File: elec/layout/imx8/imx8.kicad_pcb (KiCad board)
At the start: 2 copper layers, 67 parts, among them U1 _NXP_Semicon_MIMX8MM6CVTKZAA

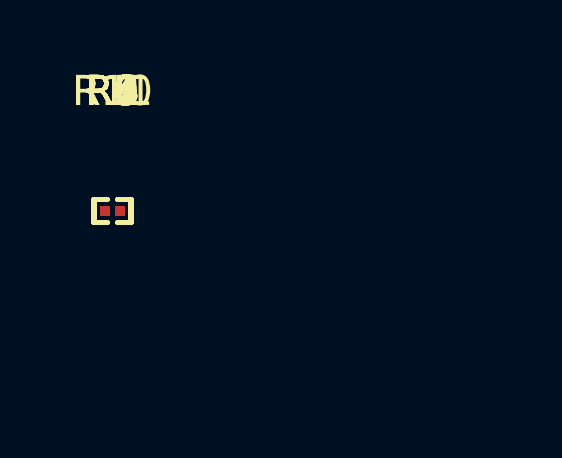
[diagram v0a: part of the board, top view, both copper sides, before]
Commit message: Update ato.yaml to build nonos + import into layout
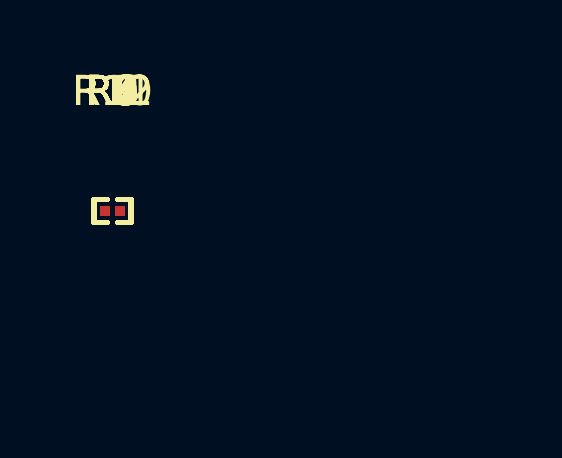
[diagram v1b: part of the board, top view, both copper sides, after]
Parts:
- added R12: 100kΩ ±1% 50mW, lcsc:R0201, F.Cu at (0.00, 0.00)
- R1: value 4.87kΩ ±1% 50mW -> 10kΩ ±1% 50mW
- R9: value 100kΩ ±1% 50mW -> 4.87kΩ ±1% 50mW
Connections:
- net *3E48.processor-net-5 renamed *7668-net-18
- net *3E48.processor.PMIC_ON_REQ-signal renamed *7668.ONOFF-signal
- net *3E48.processor.PMIC_STBY_REQ-signal renamed *7668.PMIC_ON_REQ-signal
- net NVCC_DRAM_1V1 renamed hv
- net NVCC_ENET renamed *7668-net-1
- net NVCC_SD2 renamed *7668-net-15
- net VDDA_1V8 renamed *7668-net-10
- net VDD_1V8 renamed net-0
- net VDD_3V3 renamed *7668-net-3
- net VDD_ARM_0V9 renamed *7668-net-5
- net VDD_DRAM_0V9 renamed *7668-net-2
- net VDD_PHY_0V9 renamed *7668-net-4
- net VDD_PHY_1V2 renamed *7668-net-7
- net VDD_SNVS_0V8 renamed net-1
- net VDD_SOC_0V8 renamed *7668-net-0
- net dram_ac02 renamed signal-40
- net dram_ac03 renamed signal-64
- net dram_ac04 renamed signal-8
- net dram_ac05 renamed signal-14
- net dram_ac08 renamed signal-28
- net dram_ac09 renamed signal-9
- net dram_ac10 renamed signal-43
- net dram_ac11 renamed signal-59
- net dram_ac12 renamed signal-5
- net dram_ac13 renamed signal-17
- net dram_ac22 renamed signal-18
- net dram_ac23 renamed signal-13
- net dram_ac24 renamed signal-37
- net dram_ac25 renamed signal-53
- net dram_ac28 renamed signal-62
- net dram_ac29 renamed signal-58
- net dram_ac30 renamed signal-32
- net dram_ac31 renamed signal-26
- net dram_ac32 renamed signal-65
- net dram_ac33 renamed signal-11
- net dram_dm0 renamed signal-4
- net dram_dm1 renamed signal-30
- net dram_dm2 renamed signal-22
- net dram_dm3 renamed signal-6
- net dram_dq00 renamed signal-16
- net dram_dq01 renamed signal-2
- net dram_dq02 renamed signal-23
- net dram_dq03 renamed signal-49
- net dram_dq04 renamed signal-31
- net dram_dq05 renamed signal-61
- net dram_dq06 renamed signal-55
- net dram_dq07 renamed signal-54
- net dram_dq08 renamed signal-10
- net dram_dq09 renamed signal-39
- net dram_dq10 renamed signal-38
- net dram_dq11 renamed signal-20
- net dram_dq12 renamed signal-56
- net dram_dq13 renamed signal-3
- net dram_dq14 renamed signal-47
- net dram_dq15 renamed signal-44
- net dram_dq16 renamed signal-7
- net dram_dq17 renamed signal-46
- net dram_dq18 renamed signal-66
- net dram_dq19 renamed signal-51
- net dram_dq20 renamed signal-25
- net dram_dq21 renamed signal-45
- net dram_dq22 renamed signal-33
- net dram_dq23 renamed signal-29
- net dram_dq24 renamed signal-21
- net dram_dq25 renamed signal-50
- net dram_dq26 renamed signal-1
- net dram_dq27 renamed signal-19
- net dram_dq28 renamed signal-15
- net dram_dq29 renamed signal-36
- net dram_dq30 renamed signal-60
- net dram_dq31 renamed signal-27
- net dram_dqs0_n renamed signal-67
- net dram_dqs0_p renamed signal-63
- net dram_dqs1_p renamed signal-41
- net dram_dqs3_n renamed signal-42
- net nand_ce1_b renamed *7668-signal
- net nand_ce2_b renamed signal-57
- net nand_ce3_b renamed signal-48
- net nand_cle renamed signal-0
- net nand_data04 renamed signal-34
- net nand_data05 renamed signal-24
- net nand_data06 renamed signal-52
- net nand_data07 renamed signal-12
- net nand_ready_b renamed signal-35
- C1 pad 2: GND -> lv
- C10 pad 2: GND -> lv
- C11 pad 2: GND -> lv
- C12 pad 1: *3E48.processor-hv -> *7668-hv
- C12 pad 2: GND -> lv
- C13 pad 2: GND -> lv
- C14 pad 2: GND -> lv
- C15 pad 2: GND -> lv
- C16 pad 2: GND -> lv
- C17 pad 2: GND -> lv
- C18 pad 2: GND -> lv
- C19 pad 2: GND -> lv
- C2 pad 2: GND -> lv
- C20 pad 2: GND -> lv
- C21 pad 2: GND -> lv
- C22 pad 2: GND -> lv
- C23 pad 2: GND -> lv
- C24 pad 2: GND -> lv
- C25 pad 2: GND -> lv
- C26 pad 2: GND -> lv
- C27 pad 2: GND -> lv
- C28 pad 2: GND -> lv
- C29 pad 2: GND -> lv
- C3 pad 2: GND -> lv
- C30 pad 2: GND -> lv
- C31 pad 2: GND -> lv
- C32 pad 2: GND -> lv
- C33 pad 2: GND -> lv
- C34 pad 2: GND -> lv
- C35 pad 2: GND -> lv
- C36 pad 2: GND -> lv
- C37 pad 2: GND -> lv
- C38 pad 2: GND -> lv
- C39 pad 2: GND -> lv
- C4 pad 2: GND -> lv
- C40 pad 2: GND -> lv
- C41 pad 2: GND -> lv
- C42 pad 2: GND -> lv
- C43 pad 2: GND -> lv
- C44 pad 2: GND -> lv
- C45 pad 2: GND -> lv
- C46 pad 2: GND -> lv
- C47 pad 2: GND -> lv
- C48 pad 2: GND -> lv
- C49 pad 2: GND -> lv
- C5 pad 2: GND -> lv
- C50 pad 2: GND -> lv
- C51 pad 2: GND -> lv
- C52 pad 2: GND -> lv
- C53 pad 2: GND -> lv
- C54 pad 2: GND -> lv
- C55 pad 2: GND -> lv
- C6 pad 2: GND -> lv
- C7 pad 2: GND -> lv
- C8 pad 2: GND -> lv
- C9 pad 2: GND -> lv
- R1 pad 1: *3E48.processor-net-3 -> *7668-net-6
- R1 pad 2: *3E48.processor.I2C1-hv -> lv
- R10 pad 2: *3E48.processor-hv -> *7668-hv
- R11 pad 2: *3E48.processor-hv -> *7668-hv
- R2 pad 1: *3E48.processor-net-0 -> *7668-net-11
- R2 pad 2: *3E48.processor.I2C1-hv -> *7668.I2C1-hv
- R3 pad 1: *3E48.processor-net-8 -> *7668-net-8
- R3 pad 2: *3E48.processor.I2C2-hv -> *7668.I2C1-hv
- R4 pad 1: *3E48.processor-net-2 -> *7668-net-13
- R4 pad 2: *3E48.processor.I2C2-hv -> *7668.I2C2-hv
- R5 pad 1: *3E48.processor-net-7 -> *7668-net-12
- R5 pad 2: *3E48.processor.I2C3-hv -> *7668.I2C2-hv
- R6 pad 1: *3E48.processor-net-6 -> *7668-net-9
- R6 pad 2: *3E48.processor.I2C3-hv -> *7668.I2C3-hv
- R7 pad 1: *3E48.processor-net-1 -> *7668-net-14
- R7 pad 2: *3E48.processor.I2C4-hv -> *7668.I2C3-hv
- R8 pad 1: *3E48.processor-net-4 -> *7668-net-17
- R8 pad 2: *3E48.processor.I2C4-hv -> *7668.I2C4-hv
- R9 pad 1: *3E48.processor.ONOFF-signal -> *7668-net-16
- R9 pad 2: *3E48.processor-hv -> *7668.I2C4-hv
- U1 pad A1: GND -> lv
- U1 pad A27: GND -> lv
- U1 pad AA10: GND -> lv
- U1 pad AA13: GND -> lv
- U1 pad AA15: GND -> lv
- U1 pad AA18: GND -> lv
- U1 pad AA19: GND -> lv
- U1 pad AA21: GND -> lv
- U1 pad AA7: GND -> lv
- U1 pad AA9: GND -> lv
- U1 pad AB25: GND -> lv
- U1 pad AB3: GND -> lv
- U1 pad AC25: GND -> lv
- U1 pad AC3: GND -> lv
- U1 pad AE10: GND -> lv
- U1 pad AE13: GND -> lv
- U1 pad AE14: GND -> lv
- U1 pad AE15: GND -> lv
- U1 pad AE18: GND -> lv
- U1 pad AE19: GND -> lv
- U1 pad AE2: GND -> lv
- U1 pad AE22: GND -> lv
- U1 pad AE23: GND -> lv
- U1 pad AE5: GND -> lv
- U1 pad AE6: GND -> lv
- U1 pad AE9: GND -> lv
- U1 pad AF3: GND -> lv
- U1 pad AG1: GND -> lv
- U1 pad AG27: GND -> lv
- U1 pad B26: GND -> lv
- U1 pad B3: GND -> lv
- U1 pad C10: GND -> lv
- U1 pad C13: GND -> lv
- U1 pad C14: GND -> lv
- U1 pad C15: GND -> lv
- U1 pad C18: GND -> lv
- U1 pad C19: GND -> lv
- U1 pad C2: GND -> lv
- U1 pad C22: GND -> lv
- U1 pad C23: GND -> lv
- U1 pad C5: GND -> lv
- U1 pad C6: GND -> lv
- U1 pad C9: GND -> lv
- U1 pad D10: *3E48.processor-net-8 -> *7668-net-13
- U1 pad D13: *3E48.processor-net-1 -> *7668-net-17
- U1 pad D9: *3E48.processor-net-2 -> *7668-net-12
- U1 pad E10: *3E48.processor-net-7 -> *7668-net-9
- U1 pad E13: *3E48.processor-net-4 -> *7668-net-16
- U1 pad E25: GND -> lv
- U1 pad E3: GND -> lv
- U1 pad E9: *3E48.processor-net-3 -> *7668-net-11
- U1 pad F10: *3E48.processor-net-6 -> *7668-net-14
- U1 pad F25: GND -> lv
- U1 pad F3: GND -> lv
- U1 pad F9: *3E48.processor-net-0 -> *7668-net-8
- U1 pad G10: GND -> lv
- U1 pad G13: GND -> lv
- U1 pad G15: GND -> lv
- U1 pad G18: GND -> lv
- U1 pad G19: GND -> lv
- U1 pad G21: GND -> lv
- U1 pad G7: GND -> lv
- U1 pad G9: GND -> lv
- U1 pad H18: GND -> lv
- U1 pad H2: GND -> lv
- U1 pad J21: GND -> lv
- U1 pad J22: *3E48.processor-hv -> *7668-hv
- U1 pad J25: GND -> lv
- U1 pad J3: GND -> lv
- U1 pad J7: GND -> lv
- U1 pad K20: GND -> lv
- U1 pad K21: GND -> lv
- U1 pad K25: GND -> lv
- U1 pad K3: GND -> lv
- U1 pad K7: GND -> lv
- U1 pad L12: GND -> lv
- U1 pad L16: GND -> lv
- U1 pad M12: GND -> lv
- U1 pad M16: GND -> lv
- U1 pad N12: GND -> lv
- U1 pad N16: GND -> lv
- U1 pad N21: GND -> lv
- U1 pad N25: GND -> lv
- U1 pad N3: GND -> lv
- U1 pad N7: GND -> lv
- U1 pad P13: GND -> lv
- U1 pad P15: GND -> lv
- U1 pad P21: GND -> lv
- U1 pad P25: GND -> lv
- U1 pad P3: GND -> lv
- U1 pad R1: dram_reset_n -> *7668-net-6
- U1 pad R12: GND -> lv
- U1 pad R16: GND -> lv
- U1 pad R20: GND -> lv
- U1 pad R21: GND -> lv
- U1 pad R25: GND -> lv
- U1 pad R3: GND -> lv
- U1 pad R7: GND -> lv
- U1 pad T12: GND -> lv
- U1 pad T16: GND -> lv
- U1 pad U12: GND -> lv
- U1 pad U16: GND -> lv
- U1 pad V21: GND -> lv
- U1 pad V25: GND -> lv
- U1 pad V3: GND -> lv
- U1 pad V7: GND -> lv
- U1 pad W21: GND -> lv
- U1 pad W25: GND -> lv
- U1 pad W3: GND -> lv
- U1 pad W7: GND -> lv
- U1 pad Y13: GND -> lv
- U1 pad Y18: GND -> lv
- U1 pad Y2: GND -> lv
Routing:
- net lv: track 0.00 -> 0.48 mm, vias 0 -> 35
- net GND: track 0.48 -> 0.00 mm, vias 35 -> 0

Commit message: update naming
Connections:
- net *7668-hv renamed *A7C8-hv
- net *7668-net-0 renamed *A7C8-net-0
- net *7668-net-1 renamed *A7C8-net-7
- net *7668-net-10 renamed *A7C8-net-10
- net *7668-net-11 renamed *A7C8-net-14
- net *7668-net-12 renamed *A7C8-net-18
- net *7668-net-13 renamed *A7C8-net-9
- net *7668-net-14 renamed *A7C8-net-15
- net *7668-net-15 renamed *A7C8-net-17
- net *7668-net-16 renamed *A7C8-net-4
- net *7668-net-17 renamed *A7C8-net-12
- net *7668-net-18 renamed *A7C8-net-13
- net *7668-net-2 renamed *A7C8-net-1
- net *7668-net-3 renamed *A7C8-net-5
- net *7668-net-4 renamed *A7C8-net-6
- net *7668-net-5 renamed *A7C8-net-3
- net *7668-net-6 renamed *A7C8-net-11
- net *7668-net-7 renamed *A7C8-net-8
- net *7668-net-8 renamed *A7C8-net-16
- net *7668-net-9 renamed *A7C8-net-2
- net *7668-signal renamed nand_ce1_b
- net *7668.I2C1-hv renamed *A7C8.I2C1-hv
- net *7668.I2C2-hv renamed *A7C8.I2C2-hv
- net *7668.I2C3-hv renamed *A7C8.I2C3-hv
- net *7668.I2C4-hv renamed *A7C8.I2C4-hv
- net *7668.ONOFF-signal renamed *A7C8.ONOFF-signal
- net *7668.PMIC_ON_REQ-signal renamed *A7C8.PMIC_ON_REQ-signal
- net *7668.PMIC_STBY_REQ-signal renamed *A7C8.PMIC_STBY_REQ-signal
- U1 pad A2: signal-63 -> dram_dqs0_p
- U1 pad A3: signal-55 -> signal-43
- U1 pad A4: signal-4 -> signal-5
- U1 pad A5: signal-16 -> signal-8
- U1 pad AA2: signal-46 -> signal-4
- U1 pad AB1: signal-22 -> signal-21
- U1 pad AB2: signal-7 -> signal-17
- U1 pad AC1: signal-33 -> signal-48
- U1 pad AC2: signal-29 -> signal-45
- U1 pad AC4: signal-32 -> signal-40
- U1 pad AD1: signal-19 -> signal-30
- U1 pad AD2: signal-1 -> signal-14
- U1 pad AD5: signal-26 -> signal-38
- U1 pad AE1: signal-15 -> signal-29
- U1 pad AF1: signal-36 -> signal-47
- U1 pad AF2: signal-42 -> signal-55
- U1 pad AF4: signal-27 -> signal-42
- U1 pad AF5: signal-50 -> signal-63
- U1 pad AG3: signal-60 -> signal-3
- U1 pad AG4: signal-6 -> signal-19
- U1 pad AG5: signal-21 -> signal-35
- U1 pad B1: signal-61 -> signal-0
- U1 pad B2: signal-67 -> signal-12
- U1 pad B4: signal-54 -> signal-67
- U1 pad B5: signal-2 -> signal-15
- U1 pad C1: signal-31 -> signal-39
- U1 pad D1: signal-49 -> signal-61
- U1 pad D2: signal-23 -> signal-37
- U1 pad D5: signal-59 -> signal-2
- U1 pad E1: signal-47 -> signal-57
- U1 pad E2: signal-44 -> signal-59
- U1 pad E4: signal-43 -> signal-56
- U1 pad F1: signal-30 -> signal-46
- U1 pad F2: signal-10 -> signal-23
- U1 pad G1: signal-41 -> dram_dqs1_p
- U1 pad G2: signal-39 -> signal-52
- U1 pad H1: dram_dqs1_n -> signal-27
- U1 pad J1: signal-38 -> signal-49
- U1 pad J2: signal-20 -> signal-34
- U1 pad J4: signal-64 -> signal-9
- U1 pad J6: signal-28 -> signal-44
- U1 pad K1: signal-3 -> signal-16
- U1 pad K2: signal-56 -> signal-62
- U1 pad K26: signal-52 -> signal-65
- U1 pad K27: signal-0 -> signal-13
- U1 pad K4: signal-40 -> signal-53
- U1 pad K6: signal-9 -> signal-22
- U1 pad L1: signal-14 -> signal-28
- U1 pad L2: signal-8 -> signal-18
- U1 pad L26: signal-24 -> signal-32
- U1 pad L27: signal-48 -> signal-58
- U1 pad M26: signal-34 -> signal-54
- U1 pad M27: signal-57 -> signal-6
- U1 pad N26: signal-12 -> signal-25
- U1 pad N4: signal-5 -> signal-20
- U1 pad N5: signal-17 -> signal-36
- U1 pad P26: signal-35 -> signal-50
- U1 pad R4: signal-65 -> signal-10
- U1 pad R5: signal-11 -> signal-24
- U1 pad U1: signal-53 -> signal-66
- U1 pad U2: signal-37 -> signal-51
- U1 pad V1: signal-45 -> signal-60
- U1 pad V2: signal-25 -> signal-33
- U1 pad V4: signal-13 -> signal-26
- U1 pad V6: signal-58 -> signal-1
- U1 pad W1: signal-66 -> signal-11
- U1 pad W2: signal-51 -> signal-64
- U1 pad W4: signal-18 -> signal-31
- U1 pad W6: signal-62 -> signal-7
- U1 pad Y1: dram_dqs2_n -> signal-41
